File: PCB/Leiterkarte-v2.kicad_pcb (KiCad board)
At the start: 4 copper layers, 40.3 x 85.7 mm, 56 parts

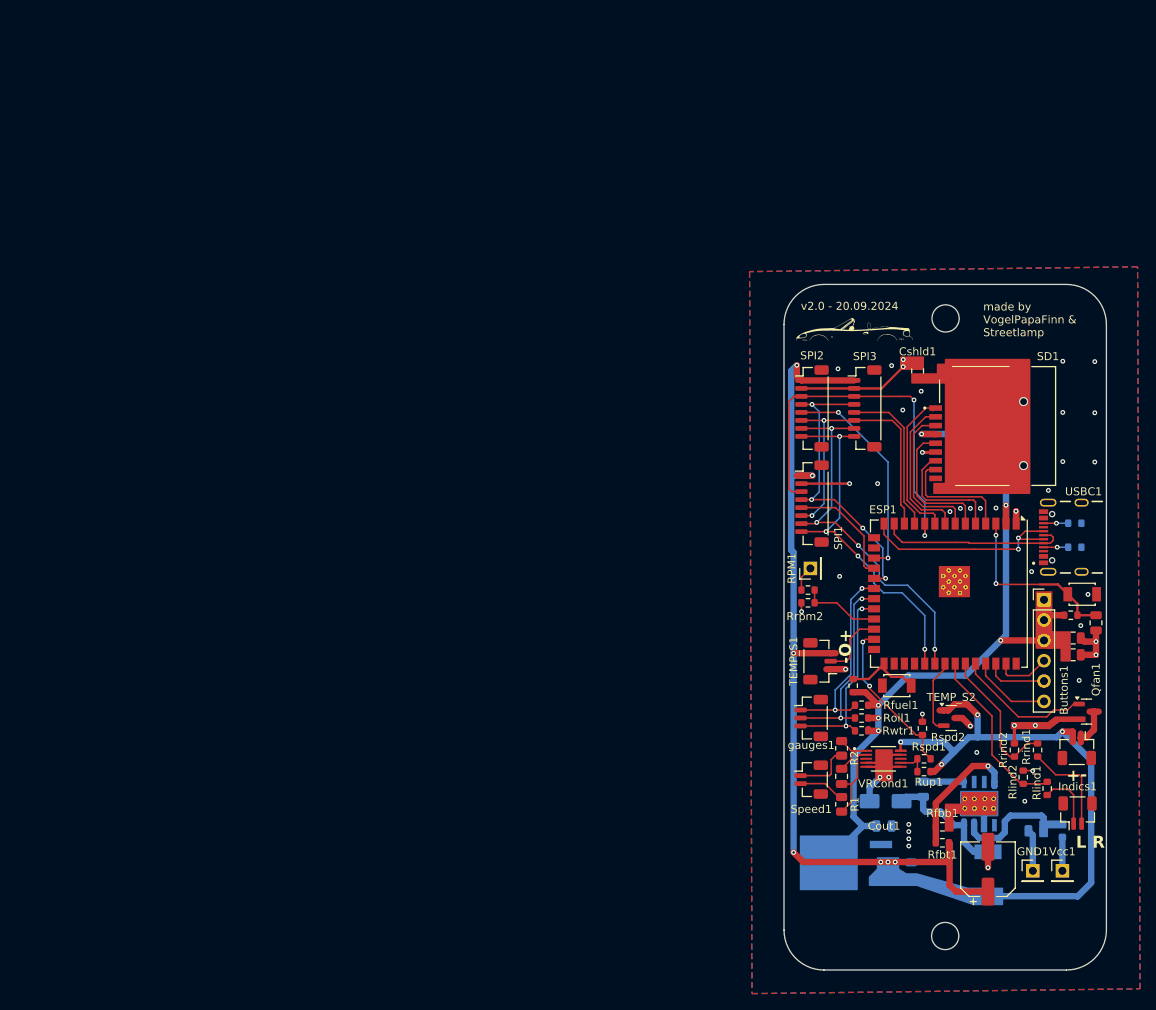
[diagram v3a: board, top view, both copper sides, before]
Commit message: Changed PCB design completely; Upgraded 3.3V regulator to 1.5A version; Removed no more needed libaries
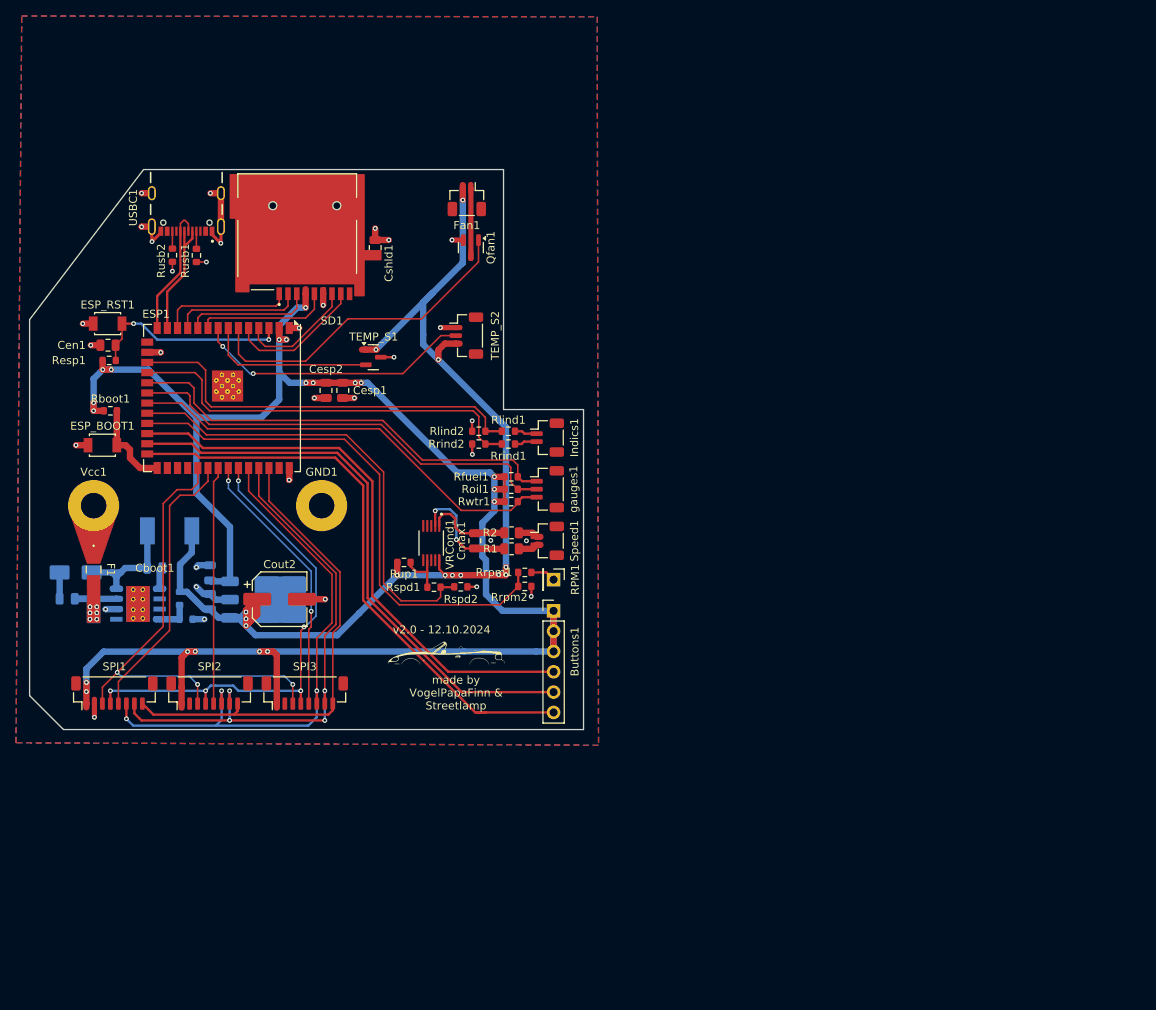
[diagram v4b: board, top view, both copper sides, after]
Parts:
- 3.3V1: value NCV33269DTRK3.3G -> LD39150DT33; footprint NCV33269DTRK3.3G:DPAK-3_ONS-M -> Package_TO_SOT_SMD:TO-252-3_TabPin2
- Cin2: value 22uF -> 10uF
- Cout1: value 10uF -> 22uF
- F1: footprint Fuse:Fuse_0603_1608Metric -> Fuse:0458Series_LTF-M; moved to F.Cu
- GND1, Vcc1: footprint Connector_PinHeader_2.54mm:PinHeader_1x01_P2.54mm_Vertical -> MountingHole:MountingHole_3.2mm_M3_Pad
- Rfbb1, Rfbt1: moved to B.Cu
- Rusb1, Rusb2: moved to F.Cu
- TEMP_S1: value Conn_01x03_Pin -> MCP9700Ax-ETT; footprint Connector_JST:JST_SH_BM03B-SRSS-TB_1x03-1MP_P1.00mm_Vertical -> Package_TO_SOT_SMD:SOT-23
- TEMP_S2: value MCP9700Ax-ETT -> Conn_01x03_Pin; footprint Package_TO_SOT_SMD:SOT-23 -> Connector_JST:JST_SH_BM03B-SRSS-TB_1x03-1MP_P1.00mm_Vertical
- moved Vcc1 129.4 mm to (58.1, 76.2)
- moved Cen1 128.3 mm to (59.9, 56.1), turned to 0 degrees
- moved ESP_RST1 126.4 mm to (59.9, 53.4), turned to 0 degrees
- moved F1 125.4 mm to (58.1, 84.1), turned to -90 degrees
- moved Cin1 124.5 mm to (54.8, 87.8)
- moved Resp1 124.3 mm to (60.0, 58.0)
- moved USBC1 119.9 mm to (69.7, 37.1), turned to 180 degrees
- moved Rusb2 117.7 mm to (68.0, 44.9), turned to -90 degrees
- moved Rusb1 115.7 mm to (71.0, 44.9), turned to -90 degrees
- moved L1 110.9 mm to (67.6, 79.3), turned to 0 degrees
- moved 5V1 108.1 mm to (63.6, 88.5), turned to 180 degrees
- moved D1 105.2 mm to (55.9, 84.5)
- moved ESP_BOOT1 103.7 mm to (59.2, 68.6)
- moved Fan1 102.6 mm to (104.8, 37.9)
- moved Rfbt1 100.1 mm to (68.8, 87.8), turned to 90 degrees
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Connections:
- 3.3V1 pad 1: GND -> +5V
- 3.3V1 pad 2: +3.3V -> GND
- 3.3V1 pad 3: +5V -> +3.3V
- Cout1 pad 1: GND -> +3.3V
- Cout1 pad 2: +3.3V -> GND
- ESP1 pad 10: DIN -> SD_CMD
- ESP1 pad 11: CS3 -> SD_DAT3
- ESP1 pad 12: DC -> SD_DAT2
- ESP1 pad 17: CS2 -> LIndicator
- ESP1 pad 18: CS1 -> RIndicator
- ESP1 pad 19: CLK -> Fuel
- ESP1 pad 20: Fuel -> Oil
- ESP1 pad 21: Oil -> WTemp
- ESP1 pad 22: WTemp -> Speed
- ESP1 pad 24: TEMP2 -> Button1
- ESP1 pad 25: Speed -> Button2
- ESP1 pad 26: GND -> Button3
- ESP1 pad 31: BL -> DIN
- ESP1 pad 32: RST -> CS1
- ESP1 pad 33: TEMP1 -> CS2
- ESP1 pad 34: LIndicator -> CS3
- ESP1 pad 35: RIndicator -> CLK
- ESP1 pad 36: FANCTRL -> DC
- ESP1 pad 37: Button3 -> RST
- ESP1 pad 38: Button2 -> BL
- ESP1 pad 39: Button1 -> unconnected-(ESP1-IO1-Pad39)
- ESP1 pad 4: SD_DAT1 -> SD_DAT0
- ESP1 pad 5: SD_DAT0 -> SD_DAT1
- ESP1 pad 6: SD_CLK -> FANCTRL
- ESP1 pad 7: SD_CMD -> TEMP1
- ESP1 pad 8: SD_DAT3 -> TEMP2
- ESP1 pad 9: SD_DAT2 -> SD_CLK
- SPI1 pad 1: +5V -> +3.3V
- SPI2 pad 1: +5V -> +3.3V
- SPI3 pad 1: +5V -> +3.3V
- TEMP_S1 pad 1: GND -> +5V
- TEMP_S1 pad 2: TEMP2 -> TEMP1
- TEMP_S1 pad 3: +5V -> GND
- TEMP_S2 pad 1: +5V -> GND
- TEMP_S2 pad 2: TEMP1 -> TEMP2
- TEMP_S2 pad 3: GND -> +5V
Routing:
- net +3.3V: track 97.0 -> 243.8 mm, vias 6 -> 20
- net Button1: track 6.90 -> 71.5 mm
- net Button2: track 7.82 -> 72.1 mm
- net Button3: track 10.1 -> 73.8 mm
- net RPM: track 9.87 -> 66.6 mm
- net Speed: track 20.1 -> 57.7 mm, vias 2 -> 0
- net +5V: track 185.5 -> 151.0 mm, vias 11 -> 13
- net RIndicator: track 18.1 -> 51.3 mm
- net DC: track 38.7 -> 70.6 mm, vias 2 -> 3
- net Oil: track 24.5 -> 55.5 mm, vias 2 -> 0
- net WTemp: track 24.2 -> 55.0 mm, vias 2 -> 0
- net Fuel: track 25.5 -> 55.7 mm, vias 2 -> 0
- net LIndicator: track 22.1 -> 51.2 mm
- net TEMP2: track 8.47 -> 35.0 mm, vias 0 -> 2
- net FANCTRL: track 17.1 -> 41.7 mm
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- added copper zone on In2.Cu, net GND
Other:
- board size 40.3 x 85.7 mm -> 69.2 x 70 mm
- board text added: "+-"
- board text added: "LR"
- board text added: "v2.0 - 12.10.2024"
- board text removed: "L R"
- board text removed: "v2.0 - 20.09.2024"

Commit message: Changed position of IGN M3 hole;Changed M3 hole diameter from 3.2 to 3.5
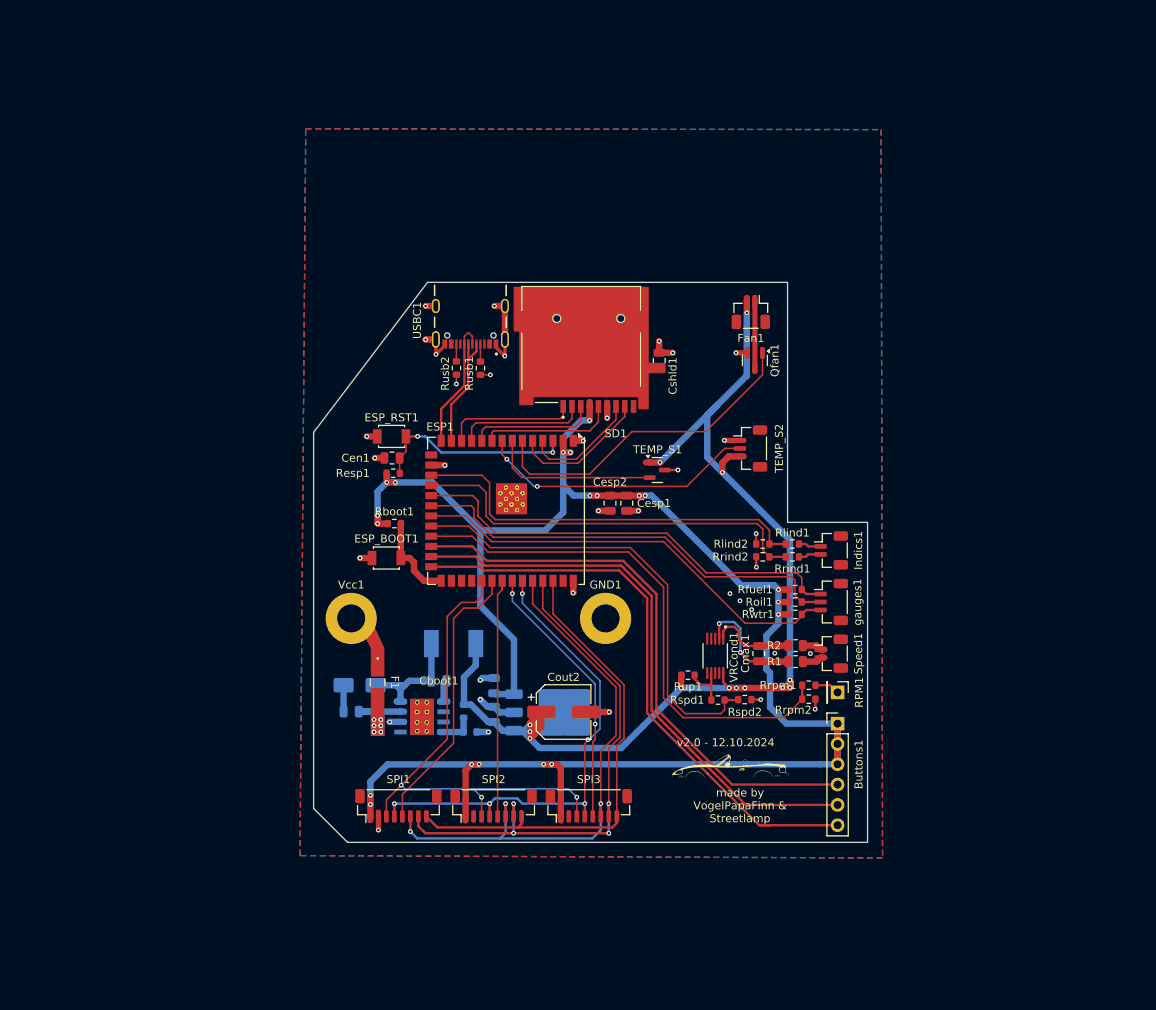
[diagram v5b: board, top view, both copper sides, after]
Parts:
- moved Cshld1 38.2 mm to (128.8, 58.0)
- moved Indics1 38.2 mm to (150.3, 81.8)
- moved Rfuel1 38.2 mm to (145.8, 86.7)
- moved Roil1 38.2 mm to (145.8, 88.2)
- moved Rwtr1 38.2 mm to (145.8, 89.8)
- moved Speed1 38.2 mm to (150.3, 94.7)
- moved VRCond1 38.2 mm to (135.8, 94.9)
- moved gauges1 38.2 mm to (150.3, 88.2)
- moved 5V1 38.2 mm to (99.2, 102.5)
- moved Buttons1 38.2 mm to (151.1, 103.4)
- moved Cen1 38.2 mm to (95.4, 70.2)
- moved Cin1 38.2 mm to (90.3, 101.9)
- moved Cmax1 38.2 mm to (141.2, 94.7)
- moved Cout1 38.2 mm to (108.2, 98.7)
- moved Cout2 38.2 mm to (116.8, 102.0)
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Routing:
- net Net-(Vcc1-Pin_1): track 5.27 -> 0.00 mm
- net GND: vias 33 -> 36
